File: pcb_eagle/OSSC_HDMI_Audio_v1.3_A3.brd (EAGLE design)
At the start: 29.8 x 17 mm, 29 parts, among them U1 PCM1808, U2 74LVC1G34, U3 MK2507SLF

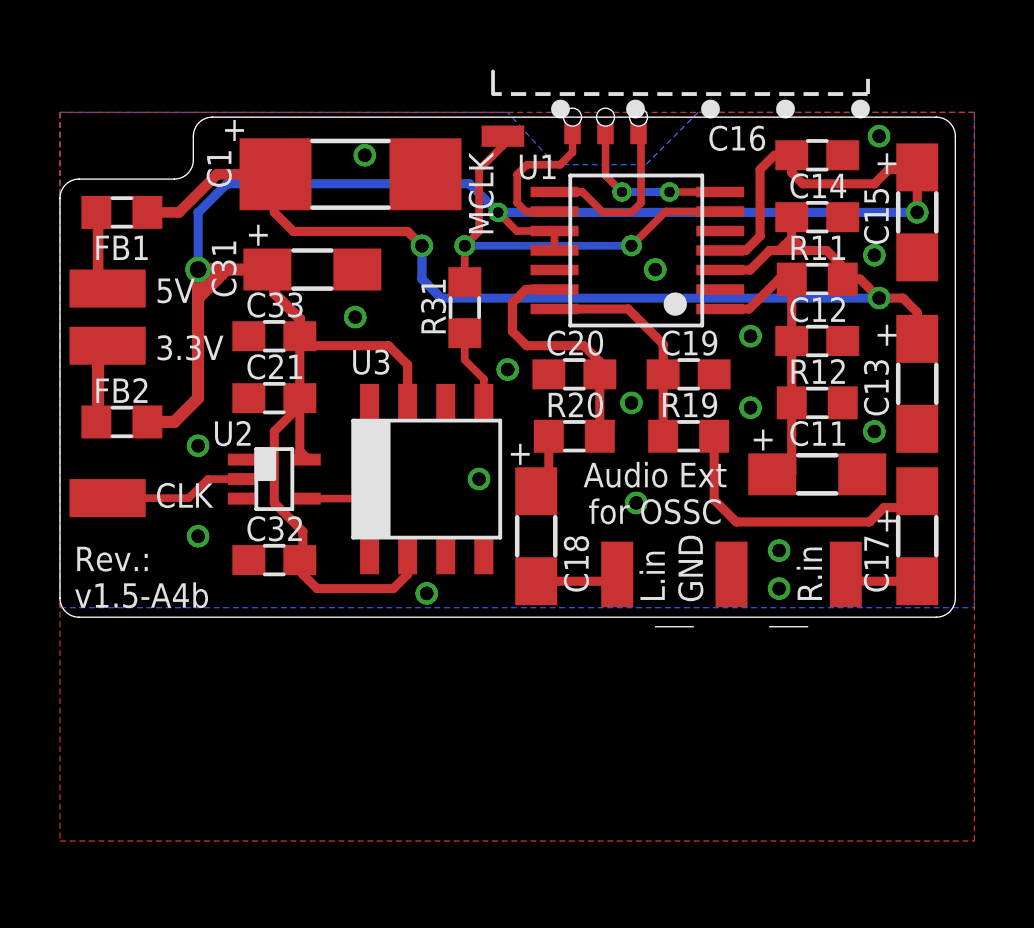
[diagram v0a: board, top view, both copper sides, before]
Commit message: External Masterclock option removed in OSSC firmware v0.75 - PCB files back to A3 - backed up A4 in additional sub-folder
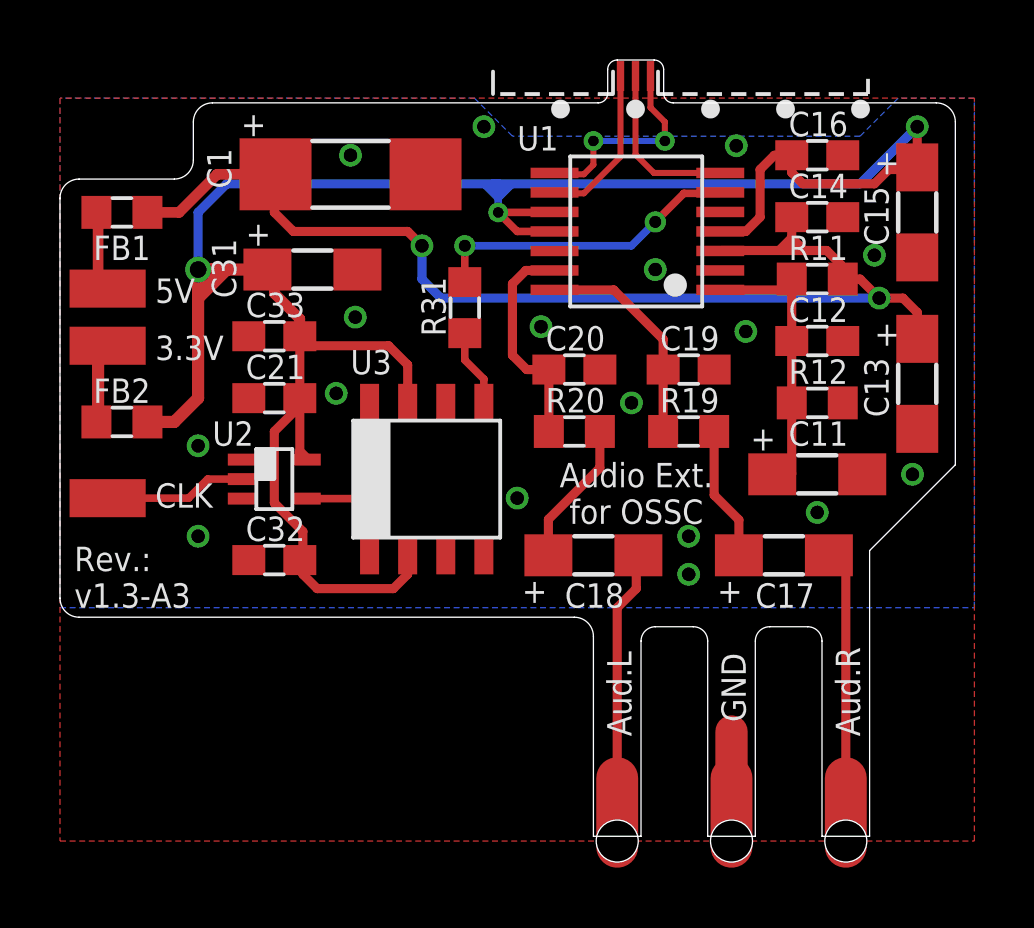
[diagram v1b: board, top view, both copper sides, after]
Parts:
- U$1: value OSSC_DIY_AUDIO_OVERLAYDIY-V1.5B -> OSSC_DIY_AUDIO_OVERLAYDIY_V1.3; device OSSC_HDMI_Audio:OSSC_OVERLAY_V1.5B -> OSSC_HDMI_Audio:OSSC_OVERLAY_V1.3
- moved C17 4.49 mm to (24.1, 9.53), turned to 0 degrees
- moved C18 2.01 mm to (17.8, 9.53), turned to 0 degrees
- moved U1 0.64 mm to (19.2, 20.3)
- moved C19 0.16 mm to (21.0, 15.7)
- moved C20 0.16 mm to (17.1, 15.7), turned to 180 degrees
- moved R19 0.16 mm to (21.0, 13.7)
- moved R20 0.16 mm to (17.1, 13.7), turned to 0 degrees
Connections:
- net N$17: no longer U$1.5
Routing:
- net N$2: track 2.48 -> 8.81 mm
- net N$1: track 2.79 -> 9.04 mm
- net N$3: track 9.85 -> 4.47 mm
- net VDD: track 75.2 -> 80.0 mm
- net GND: track 0.00 -> 3.65 mm
- net N$17: track 14.4 -> 10.8 mm
- net N$6: track 2.44 -> 4.84 mm
- net N$14: track 5.81 -> 6.98 mm, vias 0 -> 2
- net N$5: track 8.36 -> 7.44 mm
- net N$13: track 5.62 -> 5.69 mm, vias 2 -> 0
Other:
- board size 29.8 x 17 mm -> 29.8 x 25.9 mm
- board text added: "Aud.L"
- board text added: "Aud.R"
- board text added: "Audio Ext. for OSSC"
- board text added: "Rev.: v1.3-A3"
- board text removed: "Audio Ext for OSSC"
- board text removed: "L.in"
- board text removed: "MCLK"
- board text removed: "R.in"
- board text removed: "Rev.: v1.5-A4b"
